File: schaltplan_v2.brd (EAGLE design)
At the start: 100 x 80 mm, 43 parts, among them T1 2N3565, T2 2N3565, T3 2N3565, T4 2N3565, T5 2N3565, T6 2N3565, T7 2N3565, T8 2N3565, X1 SSW-102-02-S-S-RA

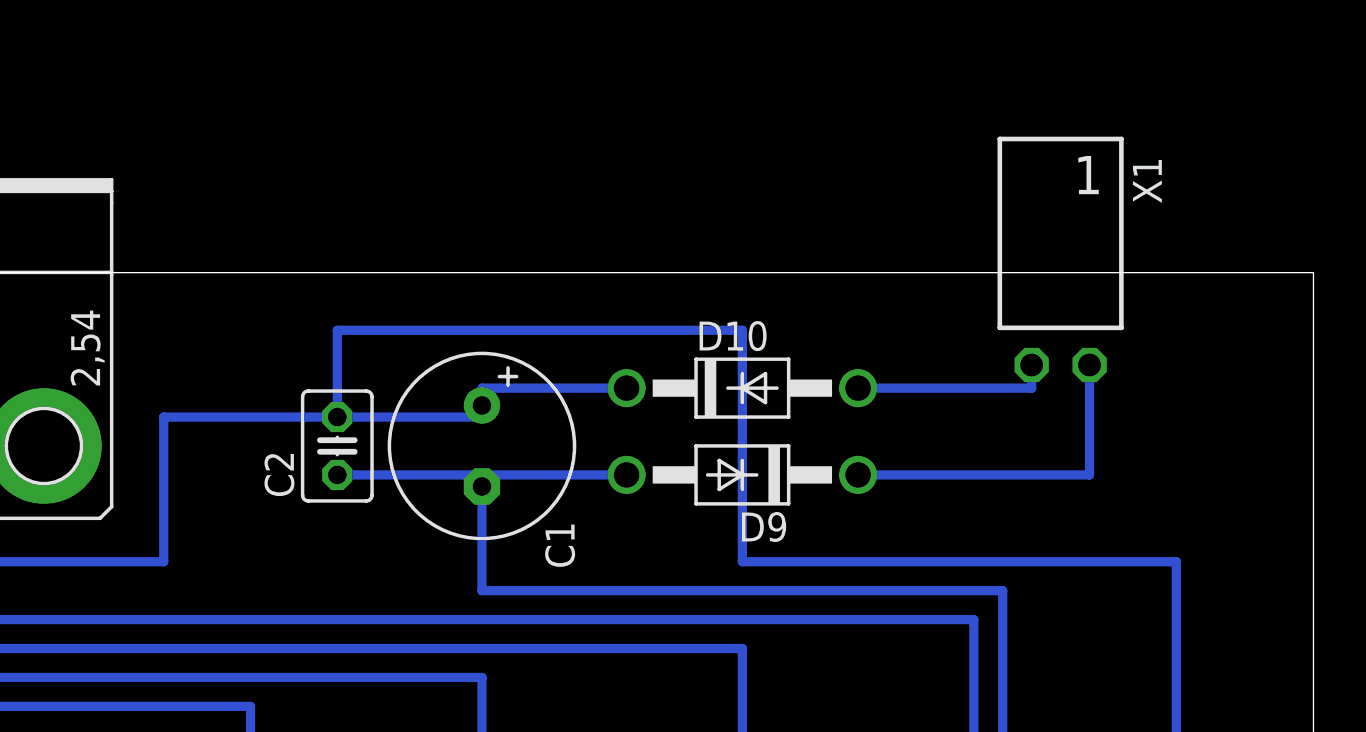
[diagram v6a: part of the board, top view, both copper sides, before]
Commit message: replaced another connector
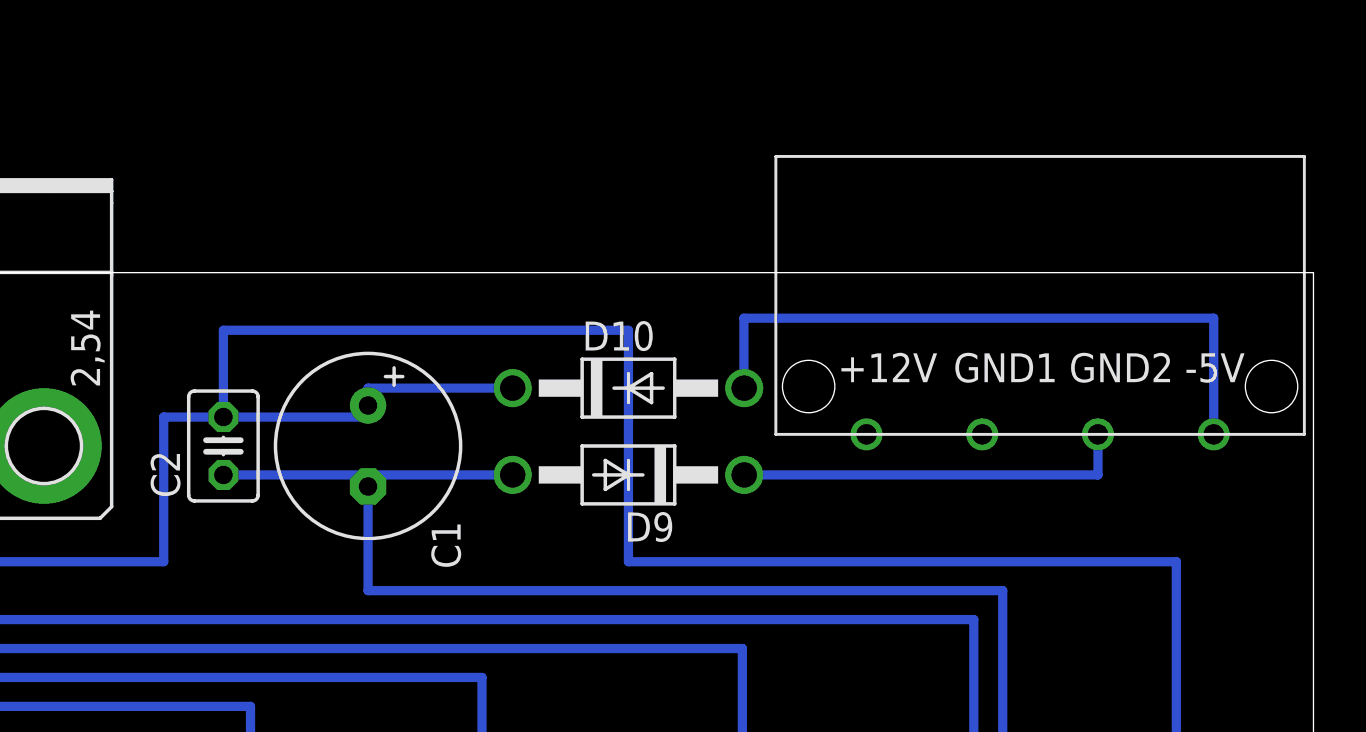
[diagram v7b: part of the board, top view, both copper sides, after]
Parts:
- removed X1: SSW-102-02-S-S-RA, con-samtec:SSW-102-02-S-S-RA
- added U$14: (no value), n39:PSW_5
- moved C1 5.00 mm to (58.5, 72.4)
- moved C2 5.00 mm to (52.1, 72.4)
- moved D10 5.00 mm to (69.9, 74.9)
- moved D9 5.00 mm to (69.9, 71.1)
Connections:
- removed net N$10: D9.C, X1.1
- removed net N$29: D10.A, X1.2
- new net N$7: D10.A, U$14.-5V
- new net N$9: D9.C, U$14.GND2
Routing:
- net N$7: track 0.00 -> 28.8 mm
- net N$9: track 0.00 -> 17.3 mm
- net N$10: track 15.0 -> 0.00 mm
- net N$29: track 8.64 -> 0.00 mm
- net N$19: track 208.5 -> 213.5 mm
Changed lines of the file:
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@@
 <element name="D2" library="diode" package="DO41-10" value="1N4004" x="78.74" y="41.91" rot="R90"/>
 <element name="T2" library="transistor" package="TO92" value="2N3565" x="74.93" y="49.53"/>
-<element name="X1" library="con-samtec" package="SSW-102-02-S-S-RA" value="SSW-102-02-S-S-RA" x="88.9" y="77.47" rot="R180">
-<attribute name="OC_NEWARK" value="11P9352" x="88.9" y="77.47" size="1.778" layer="27" rot="R180" display="off"/>
-<attribute name="MPN" value="SSW-102-02-S-S-RA" x="88.9" y="77.47" size="1.778" layer="27" rot="R180" display="off"/>
-<attribute name="MF" value="" x="88.9" y="77.47" size="1.778" layer="27" rot="R180" display="off"/>
-<attribute name="OC_FARNELL" value="unknown" x="88.9" y="77.47" size="1.778" layer="27" rot="R180" display="off"/>
-</element>
 <element name="D3" library="diode" package="DO41-10" value="1N4004" x="67.31" y="41.91" rot="R90"/>
 <element name="U$3" library="n39" package="JS_05_MN_KT" value="JS_05_MN_KT" x="58.42" y="35.56" rot="R270"/>
@@
 <element name="D8" library="diode" package="DO41-10" value="1N4004" x="13.97" y="41.91" rot="R90"/>
 <element name="T8" library="transistor" package="TO92" value="2N3565" x="10.16" y="49.53"/>
-<element name="D9" library="diode" package="DO41-10" value="1N4004" x="74.93" y="71.12" rot="R180"/>
-<element name="D10" library="diode" package="DO41-10" value="1N4004" x="74.93" y="74.93"/>
-<element name="C1" library="rcl" package="E3,5-8" value="" x="63.5" y="72.39" rot="R270"/>
-<element name="C2" library="rcl" package="C025-030X050" value="" x="57.15" y="72.39" rot="R90"/>
+<element name="D9" library="diode" package="DO41-10" value="1N4004" x="69.93" y="71.12" rot="R180"/>
+<element name="D10" library="diode" package="DO41-10" value="1N4004" x="69.93" y="74.93"/>
+<element name="C1" library="rcl" package="E3,5-8" value="" x="58.5" y="72.39" rot="R270"/>
+<element name="C2" library="rcl" package="C025-030X050" value="" x="52.15" y="72.39" rot="R90"/>
 <element name="R1" library="resistor" package="0204V" value="" x="85.09" y="55.88" rot="R270"/>
 <element name="R2" library="resistor" package="0204V" value="" x="74.93" y="55.88" rot="R270"/>
@@
 <element name="U$12" library="n39" package="WAGO_734_263" value="WAGO_734_263" x="31.75" y="-0.27" rot="R180"/>
 <element name="U$13" library="n39" package="WAGO_734_263" value="WAGO_734_263" x="10.16" y="-0.27" rot="R180"/>
+<element name="U$14" library="n39" package="PSW_5" value="" x="88" y="79"/>
 </elements>
 <signals>
@@
 <contactref element="U$8" pad="P$2"/>
 <contactref element="D8" pad="C"/>
-<wire x1="63.5" y1="74.93" x2="63.5" y2="74.168" width="0.4064" layer="16"/>
+<wire x1="58.5" y1="74.93" x2="58.5" y2="74.168" width="0.4064" layer="16"/>
 <wire x1="57.07" y1="36.83" x2="57.07" y2="33.46" width="0.4064" layer="16"/>
 <wire x1="67.13" y1="36.83" x2="67.13" y2="33.46" width="0.4064" layer="16"/>
@@
 <wire x1="78.66" y1="33.46" x2="78.74" y2="33.46" width="0.4064" layer="16"/>
 <wire x1="78.74" y1="33.46" x2="78.74" y2="36.83" width="0.4064" layer="16"/>
-<wire x1="49.53" y1="73.66" x2="57.15" y2="73.66" width="0.4064" layer="16"/>
-<wire x1="57.15" y1="73.66" x2="63.5" y2="73.66" width="0.4064" layer="16"/>
-<wire x1="63.5" y1="73.66" x2="63.5" y2="74.168" width="0.4064" layer="16"/>
-<wire x1="63.5" y1="74.93" x2="69.85" y2="74.93" width="0.4064" layer="16"/>
-<wire x1="57.15" y1="73.66" x2="57.15" y2="77.47" width="0.4064" layer="16"/>
-<wire x1="57.15" y1="77.47" x2="74.93" y2="77.47" width="0.4064" layer="16"/>
-<wire x1="74.93" y1="77.47" x2="74.93" y2="67.31" width="0.4064" layer="16"/>
-<wire x1="74.93" y1="67.31" x2="93.98" y2="67.31" width="0.4064" layer="16"/>
+<wire x1="49.53" y1="73.66" x2="52.15" y2="73.66" width="0.4064" layer="16"/>
+<wire x1="52.15" y1="73.66" x2="58.5" y2="73.66" width="0.4064" layer="16"/>
+<wire x1="58.5" y1="73.66" x2="58.5" y2="74.168" width="0.4064" layer="16"/>
+<wire x1="58.5" y1="74.93" x2="64.85" y2="74.93" width="0.4064" layer="16"/>
+<wire x1="52.15" y1="73.66" x2="52.15" y2="77.47" width="0.4064" layer="16"/>
+<wire x1="52.15" y1="77.47" x2="69.93" y2="77.47" width="0.4064" layer="16"/>
+<wire x1="69.93" y1="77.47" x2="69.93" y2="67.31" width="0.4064" layer="16"/>
+<wire x1="69.93" y1="67.31" x2="93.98" y2="67.31" width="0.4064" layer="16"/>
 <wire x1="93.98" y1="67.31" x2="93.98" y2="31.75" width="0.4064" layer="16"/>
 <wire x1="93.98" y1="31.75" x2="88.9" y2="31.75" width="0.4064" layer="16"/>
@@
 <contactref element="C1" pad="-"/>
 <contactref element="C2" pad="1"/>
-<wire x1="57.15" y1="71.12" x2="63.5" y2="71.12" width="0.4064" layer="16"/>
+<wire x1="52.15" y1="71.12" x2="58.5" y2="71.12" width="0.4064" layer="16"/>
 <contactref element="T1" pad="1"/>
 <contactref element="T2" pad="1"/>
@@
 <contactref element="T7" pad="1"/>
 <contactref element="D9" pad="A"/>
-<wire x1="69.85" y1="71.12" x2="63.5" y2="71.12" width="0.4064" layer="16"/>
-<wire x1="63.5" y1="71.12" x2="63.5" y2="66.04" width="0.4064" layer="16"/>
-<wire x1="63.5" y1="66.04" x2="86.36" y2="66.04" width="0.4064" layer="16"/>
+<wire x1="64.85" y1="71.12" x2="58.5" y2="71.12" width="0.4064" layer="16"/>
+<wire x1="58.5" y1="71.12" x2="58.5" y2="66.04" width="0.4064" layer="16"/>
+<wire x1="58.5" y1="66.04" x2="86.36" y2="66.04" width="0.4064" layer="16"/>
 <wire x1="86.36" y1="66.04" x2="86.36" y2="55.88" width="0.4064" layer="16"/>
 <wire x1="86.36" y1="55.88" x2="76.2" y2="55.88" width="0.4064" layer="16"/>
@@
 <wire x1="21.59" y1="49.53" x2="21.59" y2="55.88" width="0.4064" layer="16"/>
 <contactref element="X4" pad="G1"/>
-<wire x1="63.5" y1="71.12" x2="63.5" y2="70.612" width="0" layer="19" extent="16-16"/>
+<wire x1="58.5" y1="71.12" x2="58.5" y2="70.612" width="0" layer="19" extent="16-16"/>
 <wire x1="11.43" y1="55.88" x2="7.62" y2="55.88" width="0.4064" layer="16"/>
 <wire x1="7.62" y1="55.88" x2="7.62" y2="72.39" width="0.4064" layer="16"/>
 <wire x1="7.62" y1="72.39" x2="19.2278" y2="72.39" width="0.4064" layer="16"/>
-</signal>
-<signal name="N$29">
-<contactref element="X1" pad="2"/>
-<contactref element="D10" pad="A"/>
-<wire x1="87.63" y1="75.946" x2="87.63" y2="74.93" width="0.4064" layer="16"/>
-<wire x1="87.63" y1="74.93" x2="80.01" y2="74.93" width="0.4064" layer="16"/>
-</signal>
-<signal name="N$10">
-<contactref element="X1" pad="1"/>
-<contactref element="D9" pad="C"/>
-<wire x1="80.01" y1="71.12" x2="90.17" y2="71.12" width="0.4064" layer="16"/>
-<wire x1="90.17" y1="71.12" x2="90.17" y2="75.946" width="0.4064" layer="16"/>
 </signal>
 <signal name="N$11">
@@
 <wire x1="13.97" y1="2.27" x2="35.56" y2="2.27" width="2" layer="16"/>
 </signal>
+<signal name="N$7">
+<contactref element="U$14" pad="-5V"/>
+<contactref element="D10" pad="A"/>
+<wire x1="75.01" y1="74.93" x2="75" y2="74.93" width="0.4064" layer="16"/>
+<wire x1="75" y1="74.93" x2="75" y2="78" width="0.4064" layer="16"/>
+<wire x1="75" y1="78" x2="95.62" y2="78" width="0.4064" layer="16"/>
+<wire x1="95.62" y1="78" x2="95.62" y2="72.9" width="0.4064" layer="16"/>
+</signal>
+<signal name="N$9">
+<contactref element="U$14" pad="GND2"/>
+<contactref element="D9" pad="C"/>
+<wire x1="75.01" y1="71.12" x2="90.54" y2="71.12" width="0.4064" layer="16"/>
+<wire x1="90.54" y1="71.12" x2="90.54" y2="72.9" width="0.4064" layer="16"/>
+</signal>
 </signals>

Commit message: more layout fixes
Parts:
- removed D1, D2, D3, D4, D5, D6, D7, D8: 1N4004, diode:DO41-10
- added R10, R11, R12, R13, R14, R15, R16, R9: (no value), rcl:0207/2V
- R1, R2, R3, R4, R5, R6, R7, R8: device resistor:0204V -> rcl:0207/7
- moved T1 7.00 mm to (85.1, 42.5)
- moved T2 7.00 mm to (74.9, 42.5)
- moved T3 7.00 mm to (63.5, 42.5)
- moved T4 7.00 mm to (53.3, 42.5)
- moved T5 7.00 mm to (41.9, 42.5)
- moved T6 7.00 mm to (31.8, 42.5)
- moved T7 7.00 mm to (20.3, 42.5)
- moved T8 7.00 mm to (10.2, 42.5)
- moved R1 2.00 mm to (85.1, 53.9)
- moved R2 2.00 mm to (74.9, 53.9)
- moved R3 2.00 mm to (63.5, 53.9)
- moved R4 2.00 mm to (53.3, 53.9)
- moved R5 2.00 mm to (41.9, 53.9)
- moved R6 2.00 mm to (31.8, 53.9)
- moved R7 2.00 mm to (20.3, 53.9)
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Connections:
- new net N$10: X4.G2
- net N$12: now also R15.1; no longer D2.A
- net N$20: now also R14.1; no longer D3.A
- net N$24: now also R10.2, R11.2, R12.2, R13.2, R14.2, R15.2, R16.2, R9.2; no longer D1.C, D2.C, D3.C, D4.C, D5.C, D6.C, D7.C, D8.C
- net N$25: now also R13.1; no longer D4.A
- net N$34: now also R12.1; no longer D5.A
- net N$39: now also R11.1; no longer D6.A
- net N$46: now also R10.1; no longer D7.A
- net N$51: now also R9.1; no longer D8.A
- net N$6: now also R16.1; no longer D1.A
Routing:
- net N$19: track 213.5 -> 296.6 mm
- net N$12: track 28.8 -> 14.4 mm
- net N$34: track 28.8 -> 14.4 mm
- net N$20: track 28.9 -> 14.8 mm
- net N$6: track 23.8 -> 14.2 mm
- net N$39: track 23.8 -> 14.6 mm
- net N$25: track 23.8 -> 15.0 mm
- net N$46: track 23.8 -> 15.0 mm
- net N$51: track 23.8 -> 15.2 mm
- net N$24: track 287.7 -> 279.8 mm
- net N$8: track 3.17 -> 5.63 mm
- net N$48: track 3.17 -> 5.63 mm
- net N$40: track 3.17 -> 5.63 mm
- net N$36: track 3.17 -> 5.63 mm
- net N$28: track 3.17 -> 5.63 mm
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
